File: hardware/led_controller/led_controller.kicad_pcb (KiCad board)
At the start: 2 copper layers, 50 x 70 mm, 32 parts, among them J1 Header, J2 Header, J3 Header, J4 Header, J5 POWER, J6 Conn_01x02, U1 74AHCT125, U3 Waveshare ESP32-S3/C6 Zero

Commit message: Alignment updates
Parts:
- moved FID1 1.00 mm to (136.3, 61.4)
- moved FID2 1.00 mm to (163.2, 61.4)
- moved FID3 1.00 mm to (136.3, 95.1)
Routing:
- net DATA2: track 26.8 -> 18.7 mm
- net DATA1: track 21.3 -> 16.9 mm
- net GND: vias 17 -> 14
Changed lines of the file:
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@@
 	(footprint "Fiducial:Fiducial_1mm_Mask2mm"
 		(layer "F.Cu")
-		(at 137.3 61.4)
+		(at 136.3 61.4)
 		(descr "Fiducial, circular marking, 1mm bare copper, 2mm soldermask opening (Level A)")
 		(tags "fiducial")
@@
 	(footprint "Fiducial:Fiducial_1mm_Mask2mm"
 		(layer "F.Cu")
-		(at 163.2 62.4)
+		(at 163.2 61.4)
 		(descr "Fiducial, circular marking, 1mm bare copper, 2mm soldermask opening (Level A)")
 		(tags "fiducial")
@@
 	(footprint "Fiducial:Fiducial_1mm_Mask2mm"
 		(layer "F.Cu")
-		(at 135.3 95.1)
+		(at 136.3 95.1)
 		(descr "Fiducial, circular marking, 1mm bare copper, 2mm soldermask opening (Level A)")
 		(tags "fiducial")
@@
 	)
 	(via
-		(at 139.1 70)
-		(size 0.6)
-		(drill 0.3)
-		(layers "F.Cu" "B.Cu")
-		(free yes)
-		(net "GND")
-	)
-	(via
 		(at 139.8 86.1)
 		(size 0.6)
@@
 	)
 	(via
-		(at 138.3 70)
-		(size 0.6)
-		(drill 0.3)
-		(layers "F.Cu" "B.Cu")
-		(free yes)
-		(net "GND")
-	)
-	(via
 		(at 140.9 84.1)
 		(size 0.6)
@@
 	)
 	(via
-		(at 138.7 77)
+		(at 137.9 77)
 		(size 0.6)
 		(drill 0.3)
@@
 	)
 	(via
-		(at 138.7 76.2)
-		(size 0.6)
-		(drill 0.3)
-		(layers "F.Cu" "B.Cu")
-		(free yes)
-		(net "GND")
-	)
-	(via
-		(at 137.5 70)
+		(at 137.9 76.2)
 		(size 0.6)
 		(drill 0.3)
@@
 	)
 	(via
-		(at 138.7 77.8)
+		(at 137.9 77.8)
 		(size 0.6)
 		(drill 0.3)
@@
 	)
 	(segment
-		(start 158.3 73.89)
-		(end 161.7525 73.89)
-		(width 0.5)
-		(layer "F.Cu")
-		(net "Net-(D2-A)")
-	)
-	(segment
-		(start 161.8 73.9375)
-		(end 164.2625 73.9375)
-		(width 0.5)
-		(layer "F.Cu")
-		(net "Net-(D2-A)")
-	)
-	(segment
-		(start 155.6 76.59)
-		(end 158.3 73.89)
-		(width 0.5)
-		(layer "F.Cu")
-		(net "Net-(D2-A)")
-	)
-	(segment
-		(start 164.2625 73.9375)
-		(end 164.3 73.9)
-		(width 0.5)
-		(layer "F.Cu")
-		(net "Net-(D2-A)")
-	)
-	(segment
-		(start 155.6 78)
-		(end 155.6 76.59)
-		(width 0.5)
-		(layer "F.Cu")
-		(net "Net-(D2-A)")
-	)
-	(segment
-		(start 161.7525 73.89)
-		(end 161.8 73.9375)
-		(width 0.5)
-		(layer "F.Cu")
-		(net "Net-(D2-A)")
-	)
-	(segment
 		(start 152.675 78)
 		(end 151 78)
@@
 	)
 	(segment
-		(start 140.31 67.71)
-		(end 140.39 67.71)
-		(width 0.2)
+		(start 158.3 73.89)
+		(end 161.7525 73.89)
+		(width 0.5)
 		(layer "F.Cu")
-		(net "DATA1")
+		(net "Net-(D2-A)")
 	)
 	(segment
-		(start 134.7 70.334314)
-		(end 136.624315 68.41)
-		(width 0.2)
+		(start 161.8 73.9375)
+		(end 164.2625 73.9375)
+		(width 0.5)
 		(layer "F.Cu")
-		(net "DATA1")
+		(net "Net-(D2-A)")
 	)
 	(segment
-		(start 137.5 80.62)
-		(end 136.032819 80.62)
-		(width 0.2)
+		(start 155.6 76.59)
+		(end 158.3 73.89)
+		(width 0.5)
 		(layer "F.Cu")
-		(net "DATA1")
+		(net "Net-(D2-A)")
 	)
 	(segment
-		(start 140.31 67.79)
-		(end 140.31 67.71)
+		(start 164.2625 73.9375)
+		(end 164.3 73.9)
+		(width 0.5)
+		(layer "F.Cu")
+		(net "Net-(D2-A)")
+	)
+	(segment
+		(start 155.6 78)
+		(end 155.6 76.59)
+		(width 0.5)
+		(layer "F.Cu")
+		(net "Net-(D2-A)")
+	)
+	(segment
+		(start 161.7525 73.89)
+		(end 161.8 73.9375)
+		(width 0.5)
+		(layer "F.Cu")
+		(net "Net-(D2-A)")
+	)
+	(segment
+		(start 141.75 66.27)
+		(end 141.96 66.27)
 		(width 0.2)
 		(layer "F.Cu")
@@
 	)
 	(segment
-		(start 141.83 66.27)
-		(end 141.96 66.27)
+		(start 139 80.094999)
+		(end 139 70.994314)
 		(width 0.2)
 		(layer "F.Cu")
@@
 	)
 	(segment
-		(start 136.624315 68.41)
-		(end 139.69 68.41)
+		(start 140.31 69.684314)
+		(end 140.31 67.71)
 		(width 0.2)
 		(layer "F.Cu")
@@
 	)
 	(segment
-		(start 136.032819 80.62)
-		(end 134.7 79.287181)
+		(start 140.31 67.71)
+		(end 141.75 66.27)
 		(width 0.2)
 		(layer "F.Cu")
@@
 	)
 	(segment
-		(start 139.69 68.41)
-		(end 140.31 67.79)
+		(start 139 70.994314)
+		(end 140.31 69.684314)
 		(width 0.2)
 		(layer "F.Cu")
@@
 	)
 	(segment
-		(start 134.7 79.287181)
-		(end 134.7 70.334314)
+		(start 138.474999 80.62)
+		(end 139 80.094999)
 		(width 0.2)
 		(layer "F.Cu")
@@
 	)
 	(segment
-		(start 140.39 67.71)
-		(end 141.83 66.27)
+		(start 137.5 80.62)
+		(end 138.474999 80.62)
 		(width 0.2)
 		(layer "F.Cu")
@@
 	)
 	(segment
-		(start 138.5 79.95)
-		(end 135.95 79.95)
+		(start 138.9025 84.0025)
+		(end 139.4 83.505)
 		(width 0.2)
 		(layer "F.Cu")
@@
 	)
 	(segment
-		(start 138.9025 84.0025)
-		(end 138.9025 80.3525)
+		(start 141.75 68.81)
+		(end 141.96 68.81)
 		(width 0.2)
 		(layer "F.Cu")
@@
 	)
 	(segment
-		(start 135.1 70.5)
-		(end 136.79 68.81)
+		(start 139.4 71.16)
+		(end 141.75 68.81)
 		(width 0.2)
 		(layer "F.Cu")
@@
 	)
 	(segment
-		(start 135.95 79.95)
-		(end 135.1 79.1)
-		(width 0.2)
-		(layer "F.Cu")
-		(net "DATA2")
-	)
-	(segment
-		(start 138.9025 80.3525)
-		(end 138.5 79.95)
-		(width 0.2)
-		(layer "F.Cu")
-		(net "DATA2")
-	)
-	(segment
-		(start 135.1 79.1)
-		(end 135.1 70.5)
-		(width 0.2)
-		(layer "F.Cu")
-		(net "DATA2")
-	)
-	(segment
-		(start 136.79 68.81)
-		(end 142.51 68.81)
+		(start 139.4 83.505)
+		(end 139.4 71.16)
 		(width 0.2)
 		(layer "F.Cu")

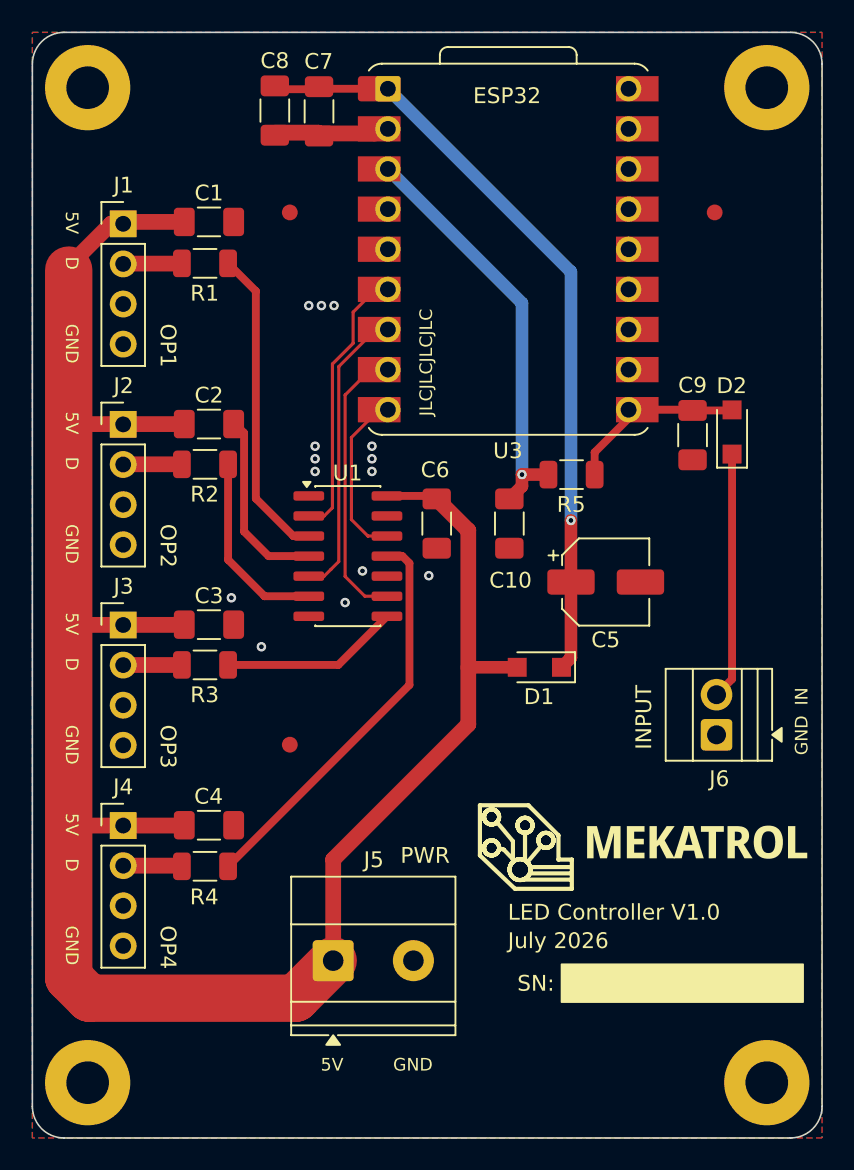
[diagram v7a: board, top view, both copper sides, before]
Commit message: Add fiducials checking
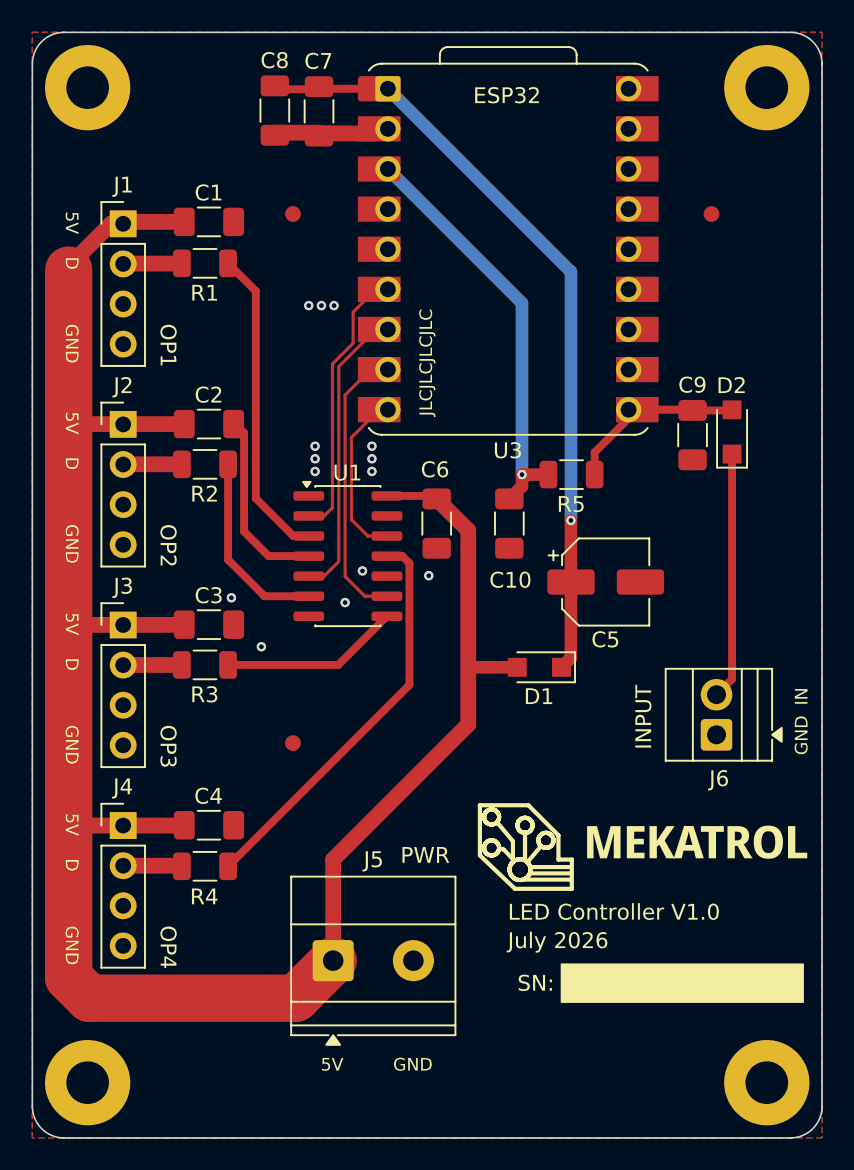
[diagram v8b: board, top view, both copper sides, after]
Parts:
- moved FID1 0.22 mm to (136.5, 61.5)
- moved FID2 0.22 mm to (163.0, 61.5)
- moved FID3 0.22 mm to (136.5, 95.0)
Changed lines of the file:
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@@
 	(footprint "Fiducial:Fiducial_1mm_Mask2mm"
 		(layer "F.Cu")
-		(at 136.3 61.4)
+		(at 136.5 61.5)
 		(descr "Fiducial, circular marking, 1mm bare copper, 2mm soldermask opening (Level A)")
 		(tags "fiducial")
@@
 		(sheetname "/")
 		(sheetfile "led_controller.kicad_sch")
-		(units
-			(unit
-				(name "A")
-				(pins)
-			)
-		)
 		(attr smd exclude_from_bom)
 		(duplicate_pad_numbers_are_jumpers no)
@@
 	(footprint "Fiducial:Fiducial_1mm_Mask2mm"
 		(layer "F.Cu")
-		(at 163.2 61.4)
+		(at 163 61.5)
 		(descr "Fiducial, circular marking, 1mm bare copper, 2mm soldermask opening (Level A)")
 		(tags "fiducial")
@@
 		(sheetname "/")
 		(sheetfile "led_controller.kicad_sch")
-		(units
-			(unit
-				(name "A")
-				(pins)
-			)
-		)
 		(attr smd exclude_from_bom)
 		(duplicate_pad_numbers_are_jumpers no)
@@
 	(footprint "Fiducial:Fiducial_1mm_Mask2mm"
 		(layer "F.Cu")
-		(at 136.3 95.1)
+		(at 136.5 95)
 		(descr "Fiducial, circular marking, 1mm bare copper, 2mm soldermask opening (Level A)")
 		(tags "fiducial")
@@
 		(sheetname "/")
 		(sheetfile "led_controller.kicad_sch")
-		(units
-			(unit
-				(name "A")
-				(pins)
-			)
-		)
 		(attr smd exclude_from_bom)
 		(duplicate_pad_numbers_are_jumpers no)
